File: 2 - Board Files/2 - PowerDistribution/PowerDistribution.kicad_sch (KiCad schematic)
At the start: 0 parts

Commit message: Added sch and pcb for initial power input stage
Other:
- company: (none) -> Periscope Robotics
- title: (none) -> Power Distribution Overview

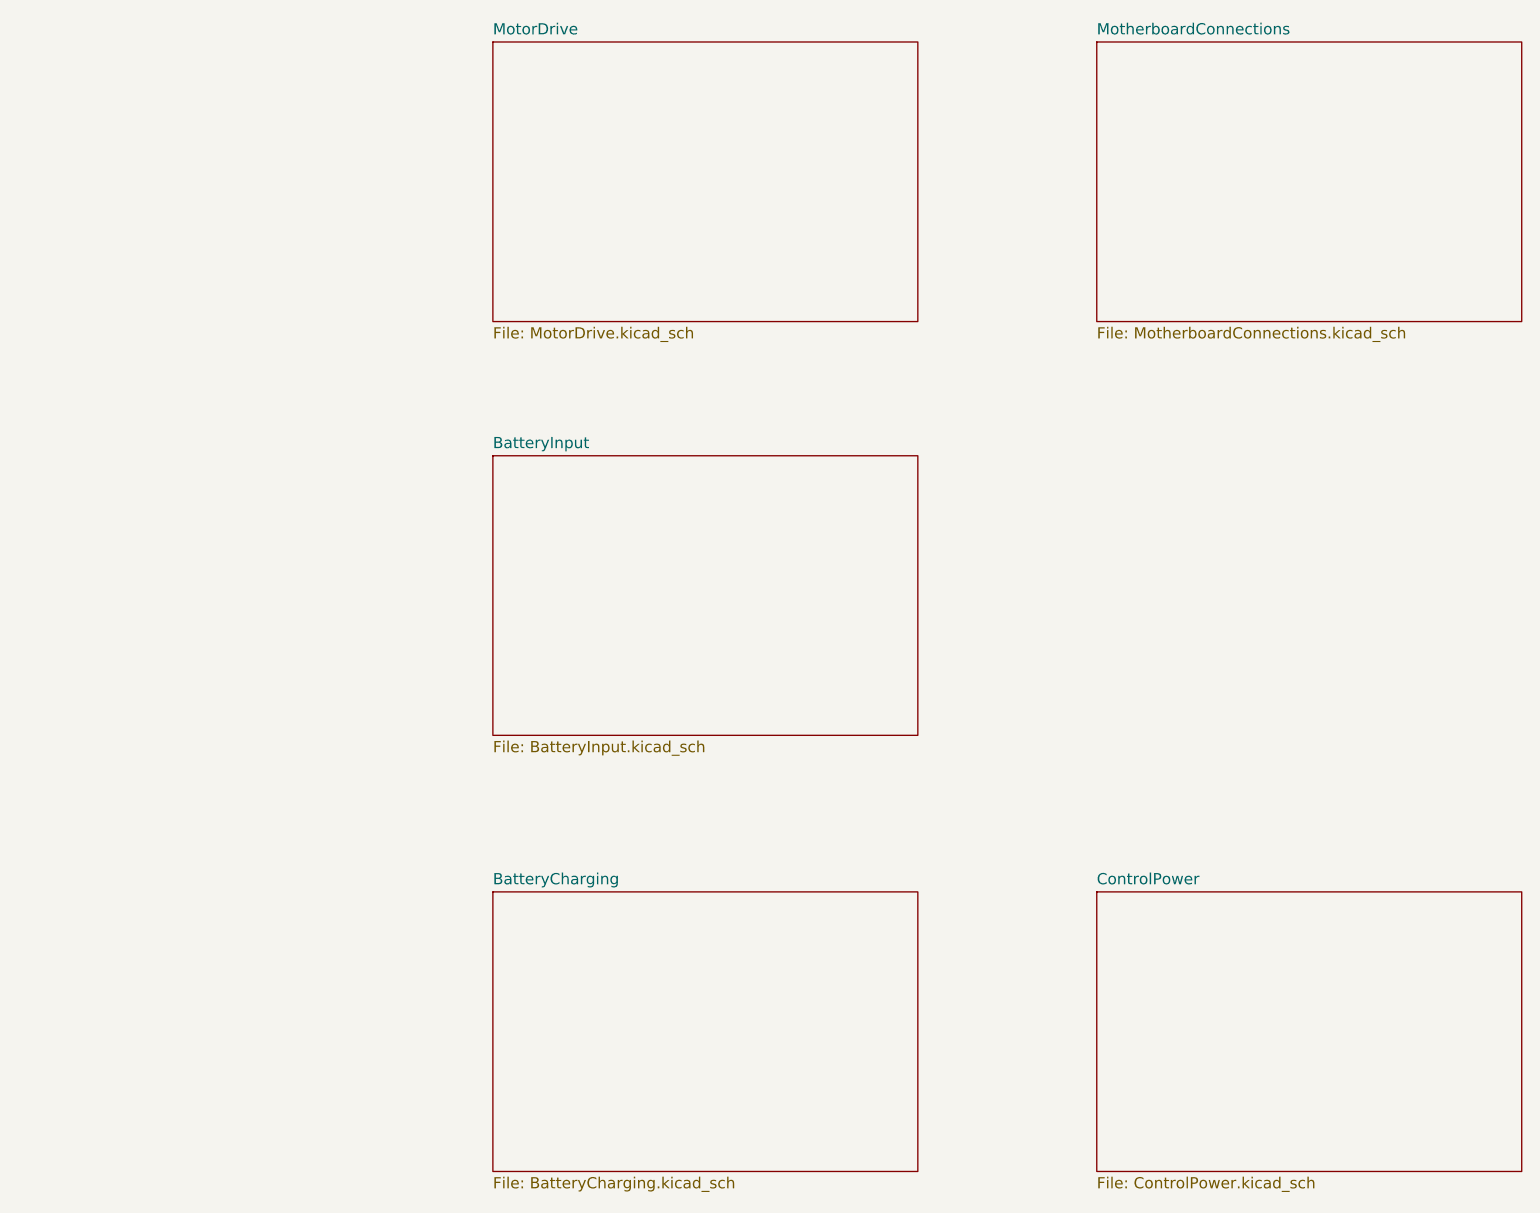
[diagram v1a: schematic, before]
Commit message: Part values for power input stage
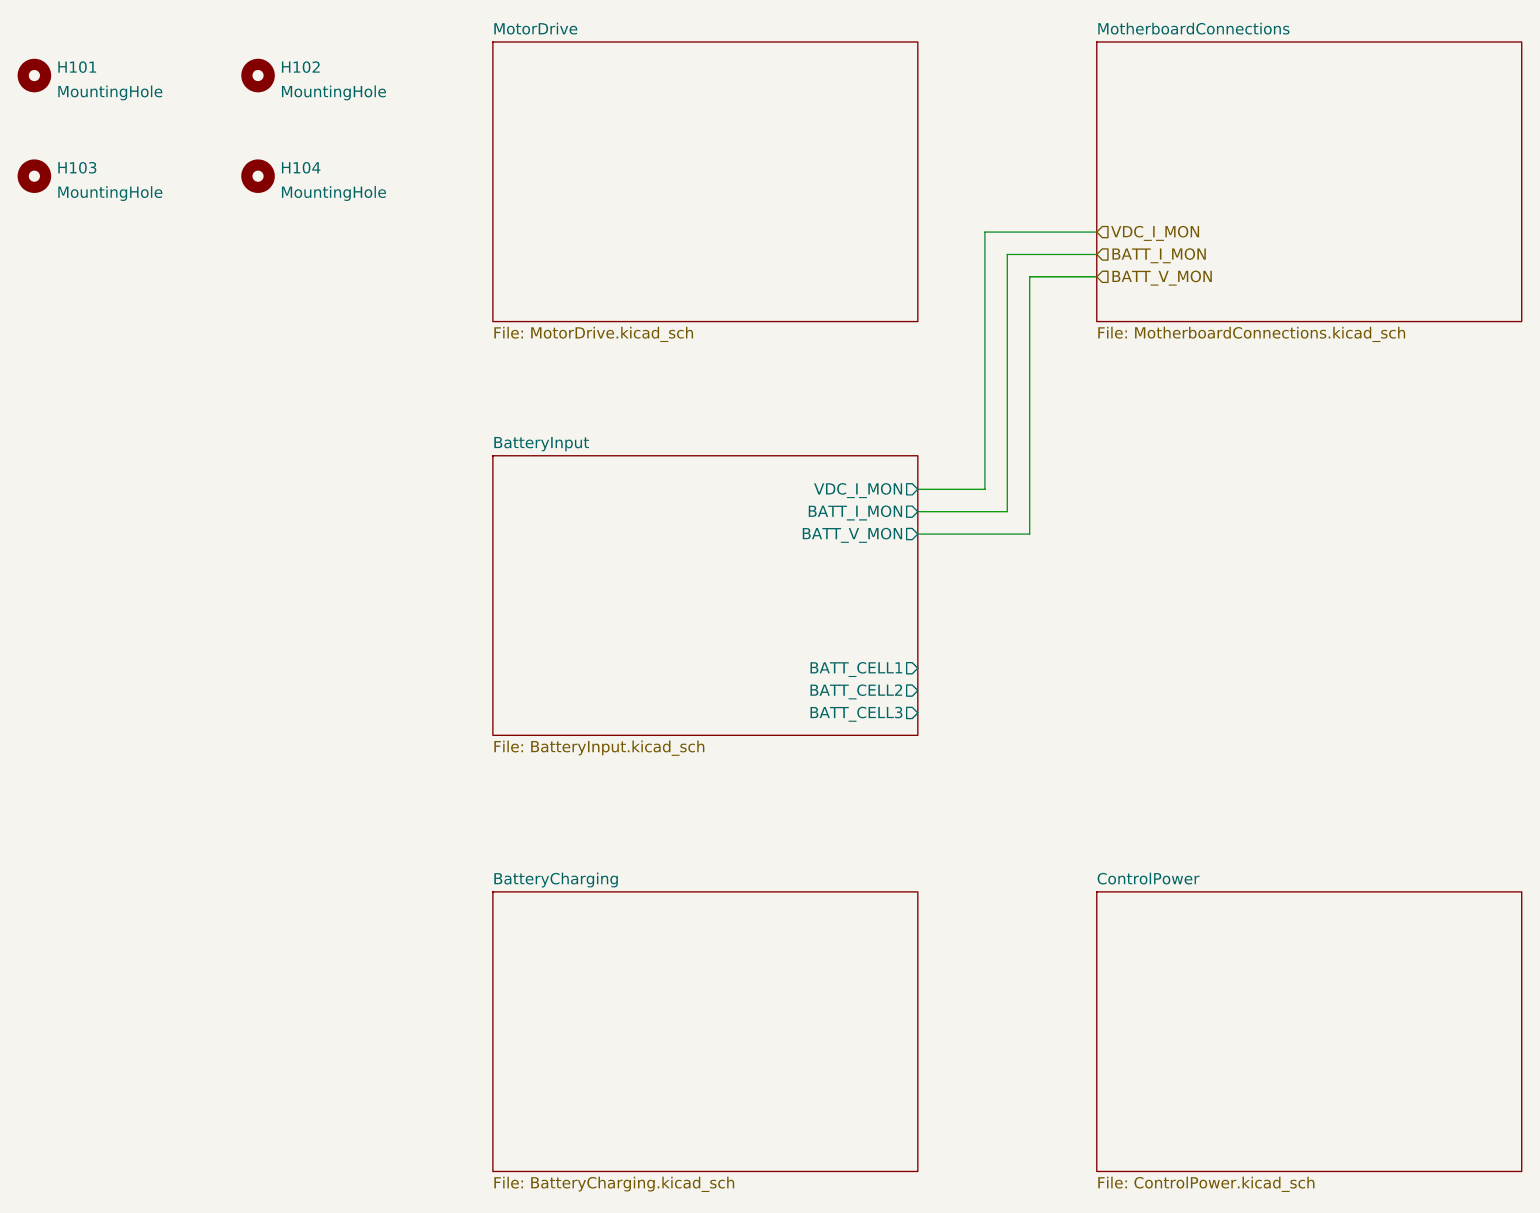
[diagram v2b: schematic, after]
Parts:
- added H101, H102, H103, H104: MountingHole, MountingHole:MountingHole_2.2mm_M2_Pad_Via, symbol Mechanical:MountingHole
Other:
- sheet BatteryInput ports: added BATT_CELL1, BATT_CELL2, BATT_CELL3, BATT_I_MON, BATT_V_MON, VDC_I_MON; removed none

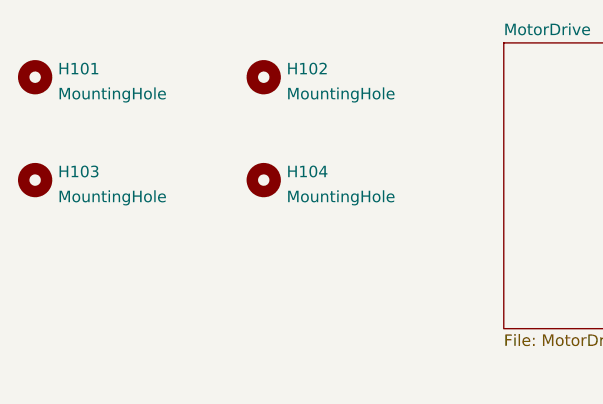
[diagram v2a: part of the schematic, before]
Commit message: Added switching regulator
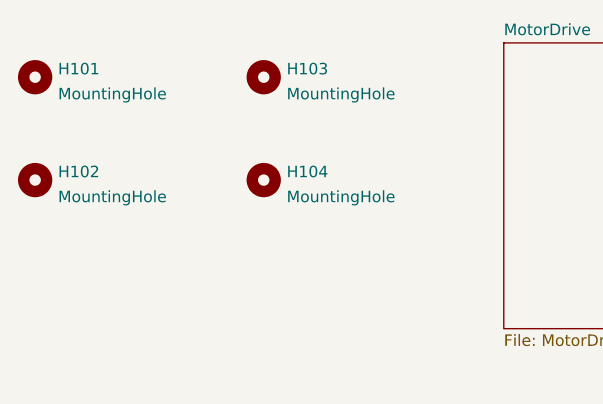
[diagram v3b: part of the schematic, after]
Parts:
- renumbered H103 to H102, H102 to H103
